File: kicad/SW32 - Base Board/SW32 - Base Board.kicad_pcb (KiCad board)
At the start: 2 copper layers, 198.1 x 99.1 mm, 91 parts, among them J1 AEXP-B, J10 TRG1, J11 TRG2, J12 FRONT_PANEL, J13 DISPLAY, J14 DRV, J15 PWR, J16 CH_IN, J17 SERIAL, J18 CH1, J19 CH2, J2 AUX1, J20 CH3, J21 CH4, J22 SERIAL_ALT, J23 PWR, J24 BAT, J3 AUX1_ALT, J4 AUX2, J5 AUX2_ALT, J6 AEXP-A, J7 I2C, J8 433TX, J9 PROG, SW1 PWR, U1 PCF8574, U2 ESP32-WROOM-32D, U3 CAT24C256, U4 SP3232, U5 LM2941, U6 TPS5430DDA, U7 NCP1117LP

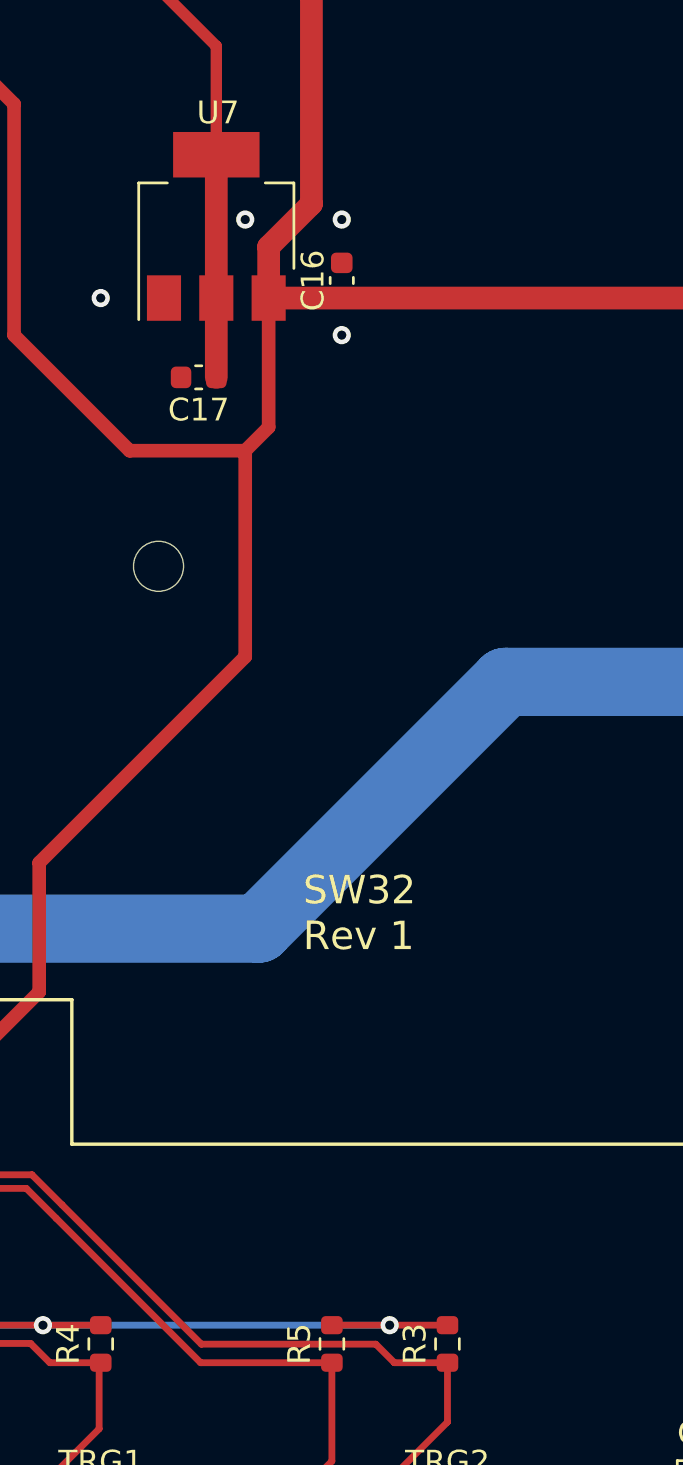
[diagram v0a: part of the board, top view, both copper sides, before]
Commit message: add power led
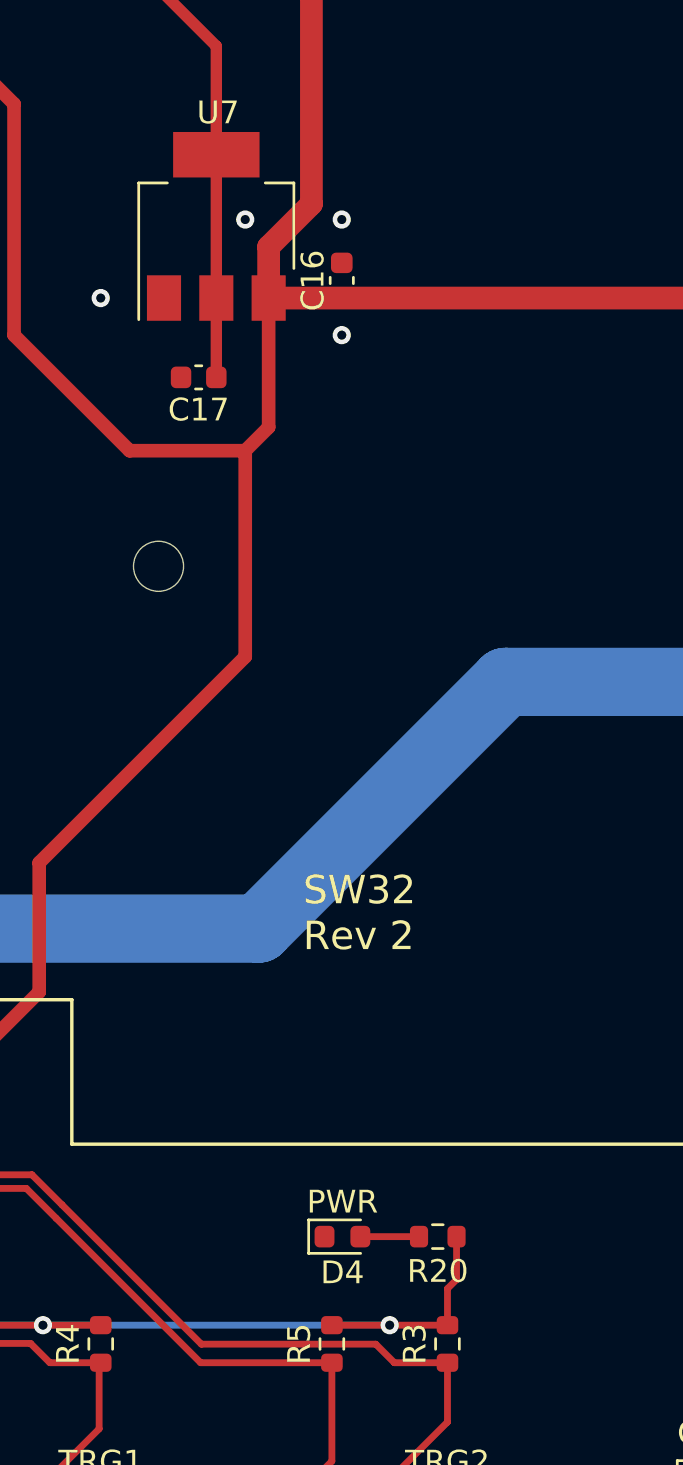
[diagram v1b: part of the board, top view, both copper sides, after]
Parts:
- added D4: PWR, LED_SMD:LED_0603_1608Metric, F.Cu at (221.4, 204.7)
- added R20: 1.5K, Resistor_SMD:R_0603_1608Metric, F.Cu at (225.6, 204.7)
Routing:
- net +3.3V: track 408.7 -> 412.7 mm
- net Net-(D4-Pad2): track 0.00 -> 2.58 mm
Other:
- board text added: "SW32 Rev 2"
- board text removed: "SW32 Rev 1"
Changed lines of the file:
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@@
   (title_block
     (title "SW32 - Base Board")
-    (date "2022-12-21")
+    (date "2022-12-23")
     (rev "2")
     (company "saawsm")
@@
   (net 118 "Net-(C14-Pad1)")
   (net 119 "Net-(C13-Pad1)")
+  (net 120 "Net-(D4-Pad2)")
   (footprint "Resistor_SMD:R_0603_1608Metric" (layer "F.Cu")
     (at 146.343317 136.747579 -90)
@@
     )
   )
+  (footprint "LED_SMD:LED_0603_1608Metric" (layer "F.Cu")
+    (at 221.44325 204.724)
+    (descr "LED SMD 0603 (1608 Metric), square (rectangular) end terminal, IPC_7351 nominal, (Body size source: http://www.tortai-tech.com/upload/download/2011102023233369053.pdf), generated with kicad-footprint-generator")
+    (tags "LED")
+    (property "MOUSER" "710-150060VS75000")
+    (property "MPN" "150060VS75000")
+    (property "Sheetfile" "power.kicad_sch")
+    (property "Sheetname" "Power Supply")
+    (attr smd)
+    (fp_text reference "D4" (at -0.000001 1.584336) (layer "F.SilkS")
+      (effects (font (size 1 1) (thickness 0.15)))
+    )
+    (fp_text value "PWR" (at 0 -1.524) (layer "F.SilkS")
+      (effects (font (size 1 1) (thickness 0.15)))
+    )
+    (fp_text user "${REFERENCE}" (at 0 0) (layer "F.Fab")
+      (effects (font (size 0.4 0.4) (thickness 0.06)))
+    )
+    (fp_line (start 0.8 -0.735) (end -1.485 -0.735) (layer "F.SilkS") (width 0.12))
+    (fp_line (start -1.485 0.735) (end 0.8 0.735) (layer "F.SilkS") (width 0.12))
+    (fp_line (start -1.485 -0.735) (end -1.485 0.735) (layer "F.SilkS") (width 0.12))
+    (fp_line (start -1.48 -0.73) (end 1.48 -0.73) (layer "F.CrtYd") (width 0.05))
+    (fp_line (start 1.48 -0.73) (end 1.48 0.73) (layer "F.CrtYd") (width 0.05))
+    (fp_line (start 1.48 0.73) (end -1.48 0.73) (layer "F.CrtYd") (width 0.05))
+    (fp_line (start -1.48 0.73) (end -1.48 -0.73) (layer "F.CrtYd") (width 0.05))
+    (fp_line (start 0.8 -0.4) (end -0.5 -0.4) (layer "F.Fab") (width 0.1))
+    (fp_line (start 0.8 0.4) (end 0.8 -0.4) (layer "F.Fab") (width 0.1))
+    (fp_line (start -0.8 -0.1) (end -0.8 0.4) (layer "F.Fab") (width 0.1))
+    (fp_line (start -0.8 0.4) (end 0.8 0.4) (layer "F.Fab") (width 0.1))
+    (fp_line (start -0.5 -0.4) (end -0.8 -0.1) (layer "F.Fab") (width 0.1))
+    (pad "1" smd roundrect (at -0.7875 0) (size 0.875 0.95) (layers "F.Cu" "F.Paste" "F.Mask") (roundrect_rratio 0.25)
+      (net 5 "GND") (pinfunction "K") (pintype "passive"))
+    (pad "2" smd roundrect (at 0.7875 0) (size 0.875 0.95) (layers "F.Cu" "F.Paste" "F.Mask") (roundrect_rratio 0.25)
+      (net 120 "Net-(D4-Pad2)") (pinfunction "A") (pintype "passive"))
+    (model "${KICAD6_3DMODEL_DIR}/LED_SMD.3dshapes/LED_0603_1608Metric.wrl"
+      (offset (xyz 0 0 0))
+      (scale (xyz 1 1 1))
+      (rotate (xyz 0 0 0))
+    )
+  )
   (footprint "Resistor_SMD:R_0603_1608Metric" locked (layer "F.Cu")
     (at 148.607274 147.459039 -90)
@@
     )
   )
+  (footprint "Resistor_SMD:R_0603_1608Metric" (layer "F.Cu")
+    (at 225.63425 204.724 180)
+    (descr "Resistor SMD 0603 (1608 Metric), square (rectangular) end terminal, IPC_7351 nominal, (Body size source: IPC-SM-782 page 72, https://www.pcb-3d.com/wordpress/wp-content/uploads/ipc-sm-782a_amendment_1_and_2.pdf), generated with kicad-footprint-generator")
+    (tags "resistor")
+    (property "LCSC" "C114668")
+    (property "MOUSER" "603-RC0603FR-071K5L")
+    (property "MPN" "RC0603FR-071K5L")
+    (property "Sheetfile" "power.kicad_sch")
+    (property "Sheetname" "Power Supply")
+    (attr smd)
+    (fp_text reference "R20" (at 0 -1.524) (layer "F.SilkS")
+      (effects (font (size 1 1) (thickness 0.15)))
+    )
+    (fp_text value "1.5K" (at 0 1.524 180) (layer "F.Fab")
+      (effects (font (size 1 1) (thickness 0.15)))
+    )
+    (fp_text user "${REFERENCE}" (at 0 0) (layer "F.Fab")
+      (effects (font (size 0.4 0.4) (thickness 0.06)))
+    )
+    (fp_line (start -0.237258 -0.5225) (end 0.237258 -0.5225) (layer "F.SilkS") (width 0.12))
+    (fp_line (start -0.237258 0.5225) (end 0.237258 0.5225) (layer "F.SilkS") (width 0.12))
+    (fp_line (start -1.48 0.73) (end -1.48 -0.73) (layer "F.CrtYd") (width 0.05))
+    (fp_line (start -1.48 -0.73) (end 1.48 -0.73) (layer "F.CrtYd") (width 0.05))
+    (fp_line (start 1.48 0.73) (end -1.48 0.73) (layer "F.CrtYd") (width 0.05))
+    (fp_line (start 1.48 -0.73) (end 1.48 0.73) (layer "F.CrtYd") (width 0.05))
+    (fp_line (start -0.8 -0.4125) (end 0.8 -0.4125) (layer "F.Fab") (width 0.1))
+    (fp_line (start 0.8 -0.4125) (end 0.8 0.4125) (layer "F.Fab") (width 0.1))
+    (fp_line (start -0.8 0.4125) (end -0.8 -0.4125) (layer "F.Fab") (width 0.1))
+    (fp_line (start 0.8 0.4125) (end -0.8 0.4125) (layer "F.Fab") (width 0.1))
+    (pad "1" smd roundrect (at -0.825 0 180) (size 0.8 0.95) (layers "F.Cu" "F.Paste" "F.Mask") (roundrect_rratio 0.25)
+      (net 6 "+3.3V") (pintype "passive"))
+    (pad "2" smd roundrect (at 0.825 0 180) (size 0.8 0.95) (layers "F.Cu" "F.Paste" "F.Mask") (roundrect_rratio 0.25)
+      (net 120 "Net-(D4-Pad2)") (pintype "passive"))
+    (model "${KICAD6_3DMODEL_DIR}/Resistor_SMD.3dshapes/R_0603_1608Metric.wrl"
+      (offset (xyz 0 0 0))
+      (scale (xyz 1 1 1))
+      (rotate (xyz 0 0 0))
+    )
+  )
   (footprint "SaawLib:STX-3100-5N" locked (layer "F.Cu")
     (at 210.82 226.06)
@@
   (gr_rect locked (start 115.57 157.48) (end 185.42 200.66) (layer "F.Fab") (width 0.1) (fill none))
   (gr_line locked (start 186.69 194.31) (end 209.55 194.31) (layer "F.Fab") (width 0.1))
-  (gr_text "SW32 \nRev 1" (at 219.71 190.5) (layer "F.SilkS")
+  (gr_text "SW32 \nRev 2" (at 219.71 190.5) (layer "F.SilkS")
     (effects (font (size 1.25 1.25) (thickness 0.25)) (justify left))
   )
@@
   (segment locked (start 180.34 162.935168) (end 180.335651 162.930819) (width 0.5) (layer "F.Cu") (net 6))
   (segment locked (start 201.93 138.43) (end 215.9 152.4) (width 0.5) (layer "F.Cu") (net 6))
+  (segment (start 226.06 207.01) (end 226.06 208.61575) (width 0.3) (layer "F.Cu") (net 6))
   (segment locked (start 159.58021 183.515) (end 159.575 183.50979) (width 0.5) (layer "F.Cu") (net 6))
   (segment locked (start 179.094147 162.930819) (end 179.07 162.954966) (width 0.5) (layer "F.Cu") (net 6))
@@
   (segment locked (start 168.929435 183.515) (end 162.99 183.515) (width 0.5) (layer "F.Cu") (net 6))
   (segment locked (start 226.06 208.61575) (end 223.52 208.61575) (width 0.3) (layer "F.Cu") (net 6))
-  (segment locked (start 215.9 156.87) (end 215.9 166.956608) (width 1) (layer "F.Cu") (net 6))
+  (segment locked (start 215.9 156.87) (end 215.9 166.956608) (width 0.5) (layer "F.Cu") (net 6))
   (segment locked (start 170.647482 172.96817) (end 168.91 174.705652) (width 0.5) (layer "F.Cu") (net 6))
   (segment locked (start 179.07 139.7) (end 180.34 138.43) (width 0.5) (layer "F.Cu") (net 6))
@@
   (segment locked (start 184.786546 138.43) (end 201.93 138.43) (width 0.5) (layer "F.Cu") (net 6))
   (segment locked (start 168.91 174.705652) (end 168.91 183.495565) (width 0.5) (layer "F.Cu") (net 6))
+  (segment (start 226.45925 204.724) (end 226.45925 206.61075) (width 0.3) (layer "F.Cu") (net 6))
   (segment locked (start 183.539545 170.790455) (end 181.36183 172.96817) (width 0.5) (layer "F.Cu") (net 6))
   (segment locked (start 147.517455 135.922579) (end 148.314479 135.125555) (width 0.3) (layer "F.Cu") (net 6))
@@
   (segment locked (start 152.753602 130.57298) (end 151.394112 130.57298) (width 0.3) (layer "F.Cu") (net 6))
   (segment locked (start 147.32 161.29) (end 147.32 163.404698) (width 0.4) (layer "F.Cu") (net 6))
+  (segment (start 226.45925 206.61075) (end 226.06 207.01) (width 0.3) (layer "F.Cu") (net 6))
   (segment locked (start 184.768868 138.43) (end 182.88 138.43) (width 0.5) (layer "F.Cu") (net 6))
   (segment locked (start 124.6 154.016791) (end 123.825 153.241791) (width 0.5) (layer "F.Cu") (net 6))
@@
   (segment locked (start 276.479 145.161) (end 276.82373 145.50573) (width 0.3) (layer "F.Cu") (net 119))
   (segment locked (start 276.82373 145.50573) (end 276.82373 149.47573) (width 0.3) (layer "F.Cu") (net 119))
+  (segment (start 224.80925 204.724) (end 222.23075 204.724) (width 0.3) (layer "F.Cu") (net 120))
   (zone locked (net 117) (net_name "Net-(C13-Pad2)") (layer "F.Cu") (hatch edge 0.508)
     (priority 1)
